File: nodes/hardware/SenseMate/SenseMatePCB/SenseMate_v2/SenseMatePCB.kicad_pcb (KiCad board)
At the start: 2 copper layers, 32.8 x 61.9 mm, 22 parts, among them J1 Conn_01x04, J2 Conn_01x12_Pin, J3 Conn_Coaxial, J4 Conn_01x06_Pin, J5 Conn_01x06_Pin, J6 Conn_01x02_Pin, J7 Conn_01x04_Pin, M1 Motor_DC, Q3 SS8050, Q4 SS8050, SW5 SW_DPDT_x2, U1 XIAO-nRF52840-Plus-SMD, U2 RFM95W-868S2

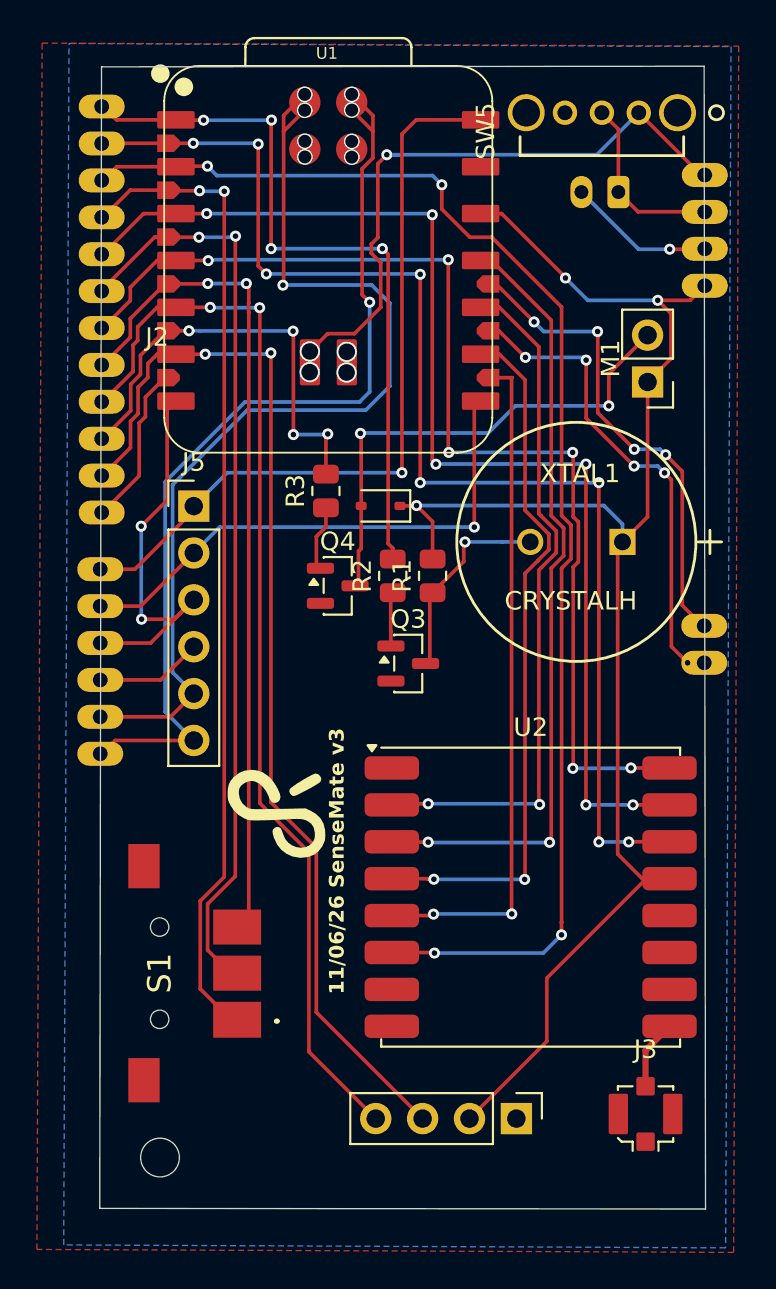
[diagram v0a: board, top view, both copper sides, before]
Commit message: nodes/firmware: tried to clean drc errors and warnings
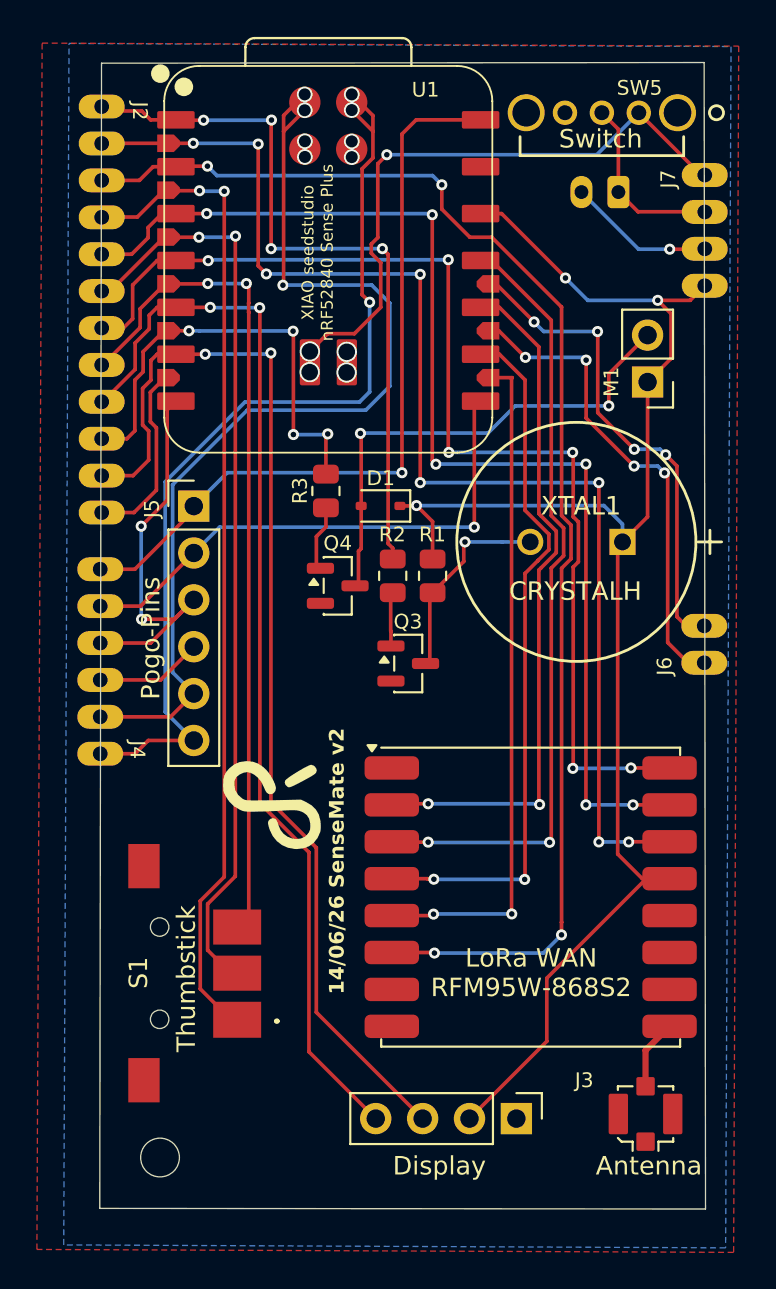
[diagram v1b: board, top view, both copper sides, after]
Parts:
- U2: value RFM95W-868S2 -> LoRa WAN
- moved G*** 0.53 mm to (98.2, 64.5)
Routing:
- net P0.31: track 8.91 -> 10.2 mm
- net SCL: track 58.9 -> 60.1 mm
- net SPI_MISO1: track 25.4 -> 26.3 mm, vias 5 -> 4
- net VBAT: track 33.9 -> 33.1 mm
- net VIB_EN: track 23.9 -> 24.7 mm
- net LoRa_DIO2: track 60.5 -> 61.1 mm
- net SPI_MOSI1: track 26.1 -> 26.7 mm
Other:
- board size 32.8 x 61.9 mm -> 32.8 x 62.1 mm
- board text added: "14/06/26 SenseMate v2"
- board text added: "Antenna"
- board text added: "Display"
- board text added: "J4"
- board text added: "J6"
- board text added: "J7"
- board text added: "Pogo-Pins"
- board text added: "RFM95W-868S2"
- board text added: "Switch"
- board text added: "Thumbstick"
- board text added: "XIAO seedstudio nRF52840 Sense Plus"
- board text removed: "11/06/26 SenseMate v3"

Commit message: hardware/SenseMate_v2: Finished Design and created gerber files
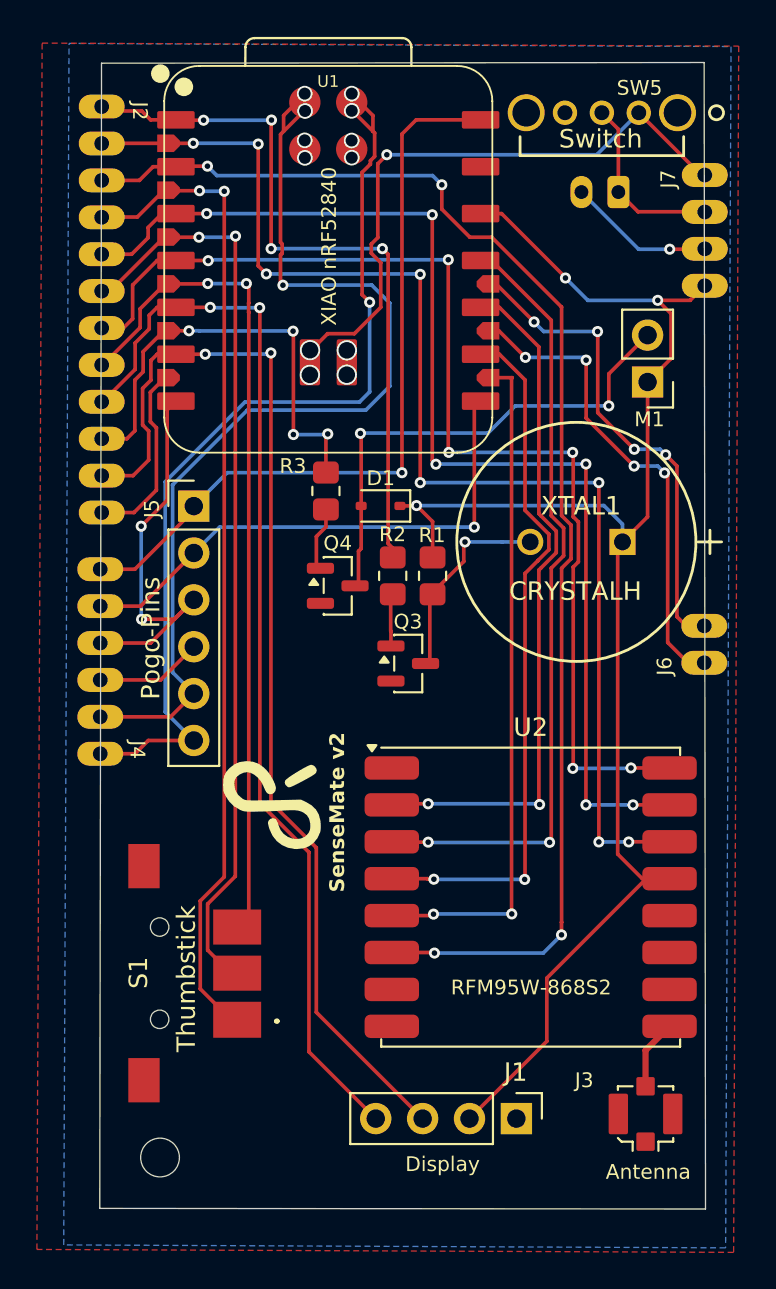
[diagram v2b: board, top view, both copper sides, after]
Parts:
- R1, R2, R3: footprint Resistor_SMD:R_0805_2012Metric -> Resistor_SMD:R_0805_2012Metric_Pad1.20x1.40mm_HandSolder
- S1: footprint SenseMate_sw_fp:COM08184 -> SenseMateLibrary:ThumbWheel
- U2: footprint RF_Module:HOPERF_RFM9XW_SMD -> SenseMateLibrary:HOPERF_RFM9XW_SMD
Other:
- copper layers 2 -> 4
- board text added: "SenseMate v2"
- board text added: "XIAO nRF52840"
- board text removed: "14/06/26 SenseMate v2"
- board text removed: "XIAO seedstudio nRF52840 Sense Plus"

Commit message: hardware/SenseMate_v2: corrected Edge Cuts and created new gerber files
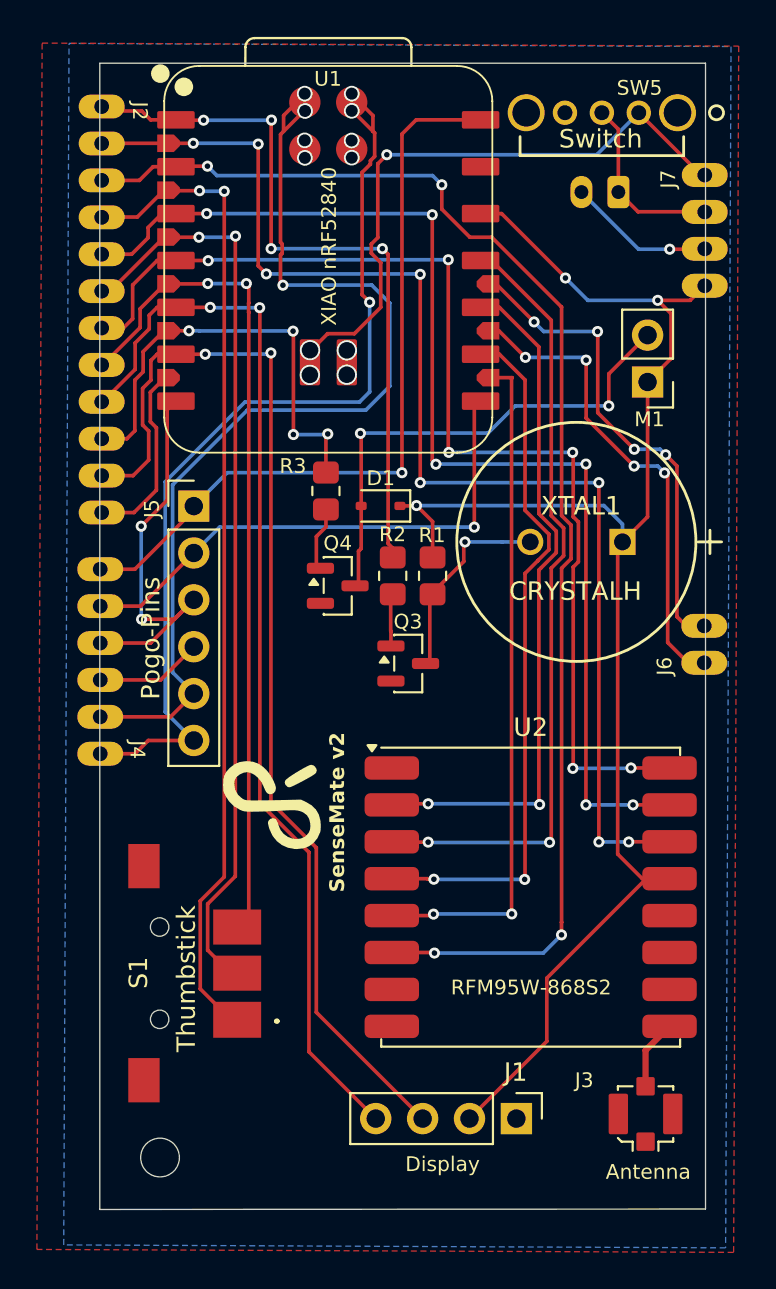
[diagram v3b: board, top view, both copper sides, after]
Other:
- outline, holes or cut-outs redrawn
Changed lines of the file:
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@@
 		(13 "F.Paste" user)
 		(15 "B.Paste" user)
-		(5 "F.SilkS" user)
-		(7 "B.SilkS" user)
+		(5 "F.SilkS" user "F.Silkscreen")
+		(7 "B.SilkS" user "B.Silkscreen")
 		(1 "F.Mask" user)
 		(3 "B.Mask" user)
 		(25 "Edge.Cuts" user)
 		(27 "Margin" user)
-		(31 "F.CrtYd" user)
-		(29 "B.CrtYd" user)
+		(31 "F.CrtYd" user "F.Courtyard")
+		(29 "B.CrtYd" user "B.Courtyard")
 		(35 "F.Fab" user)
 	)
@@
 		(capping no)
 		(filling no)
-		(zone_defaults)
 		(pcbplotparams
 			(layerselection 0x00000000_00000000_55555555_5755f5ff)
@@
 		(at 101.3072 37.5 90)
 		(property "Reference" "U1"
-			(at 9.7 -0.0072 0)
+			(at 9.84 -0.0172 0)
 			(unlocked yes)
 			(layer "F.SilkS")
 			(effects
 				(font
-					(size 0.635 0.635)
+					(size 0.8 0.8)
 					(thickness 0.1016)
 				)
@@
 	)
 	(gr_line
-		(start 88.925 88.866)
-		(end 89.020307 26.81)
+		(start 88.925 88.925)
+		(end 88.925 26.81)
 		(stroke
 			(width 0.058206)
@@
 	)
 	(gr_line
-		(start 88.925 88.866)
+		(start 88.925 88.925)
 		(end 121.75 88.9)
 		(stroke
@@
 	)
 	(gr_line
-		(start 121.675057 26.77313)
-		(end 89.02 26.81)
+		(start 121.75 26.81)
+		(end 88.93 26.81)
 		(stroke
 			(width 0.070379)
@@
 	)
 	(gr_line
-		(start 121.75 88.9)
-		(end 121.675057 26.77313)
+		(start 121.75 88.89)
+		(end 121.75 26.81)
 		(stroke
 			(width 0.070379)

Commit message: hardware/SenseMate_v2: added lables to pins, and solved some warnings and errors
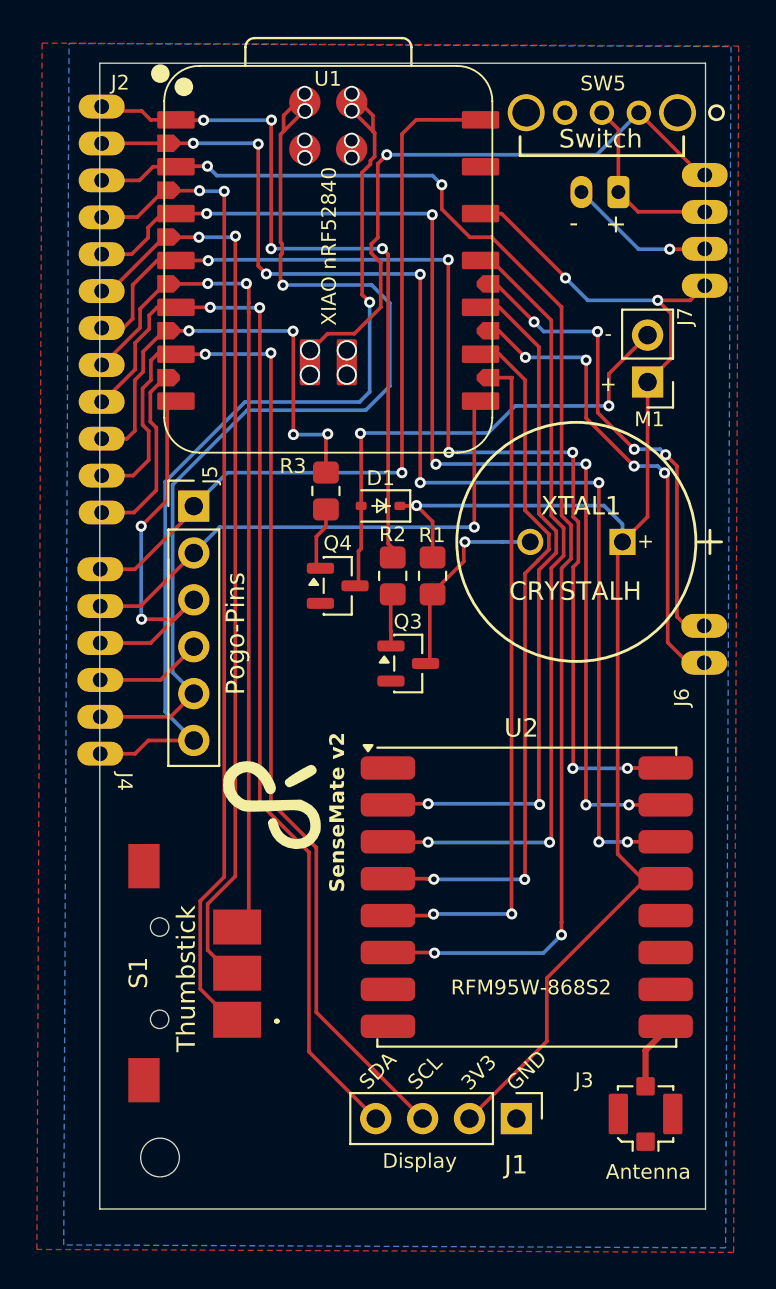
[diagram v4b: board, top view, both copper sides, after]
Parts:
- moved U2 0.21 mm to (112.1, 72.0)
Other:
- board text added: "+"
- board text added: "-"
- board text added: "3V3"
- board text added: "BAT"
- board text added: "BUZ (P0.02)"
- board text added: "DIO0 (P0.15)"
- board text added: "DIO1 (P0.28)"
- board text added: "DIO2 (P0.29)"
- board text added: "GND"
- board text added: "MISO1 (P1.07)"
- board text added: "MOSI1 (P1.05)"
- board text added: "RST (P0.03)"
- board text added: "RX (P1.12)"
- board text added: "SCL"
- board text added: "SCL (P0.05)"
- board text added: "SDA"
- board text added: "SDA (P0.04)"
- board text added: "SWDCLK"
- board text added: "SWDDIO"
- board text added: "TMB1 (P0.19)"
- board text added: "TMB2 (P0.09)"
- board text added: "TMBT1 (P1.01)"
- board text added: "TX (P1.11)"
- board text added: "VBAT"
- board text added: "VBUS"
- board text added: "VIB (P0.10)"
